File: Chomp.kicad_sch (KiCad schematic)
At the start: 47 parts, among them J1 IN2, J10 V1-6, J11 V1-8, J12 V2-5, J13 V2-8, J14 V2-4, J15 T1-4, J16 T1-2, J2 IN1, J3 V1-2, J4 V1-1, J5 V1-3, J6 RV1-1, J7 RV1-3, J8 RV1-2, J9 V1-7

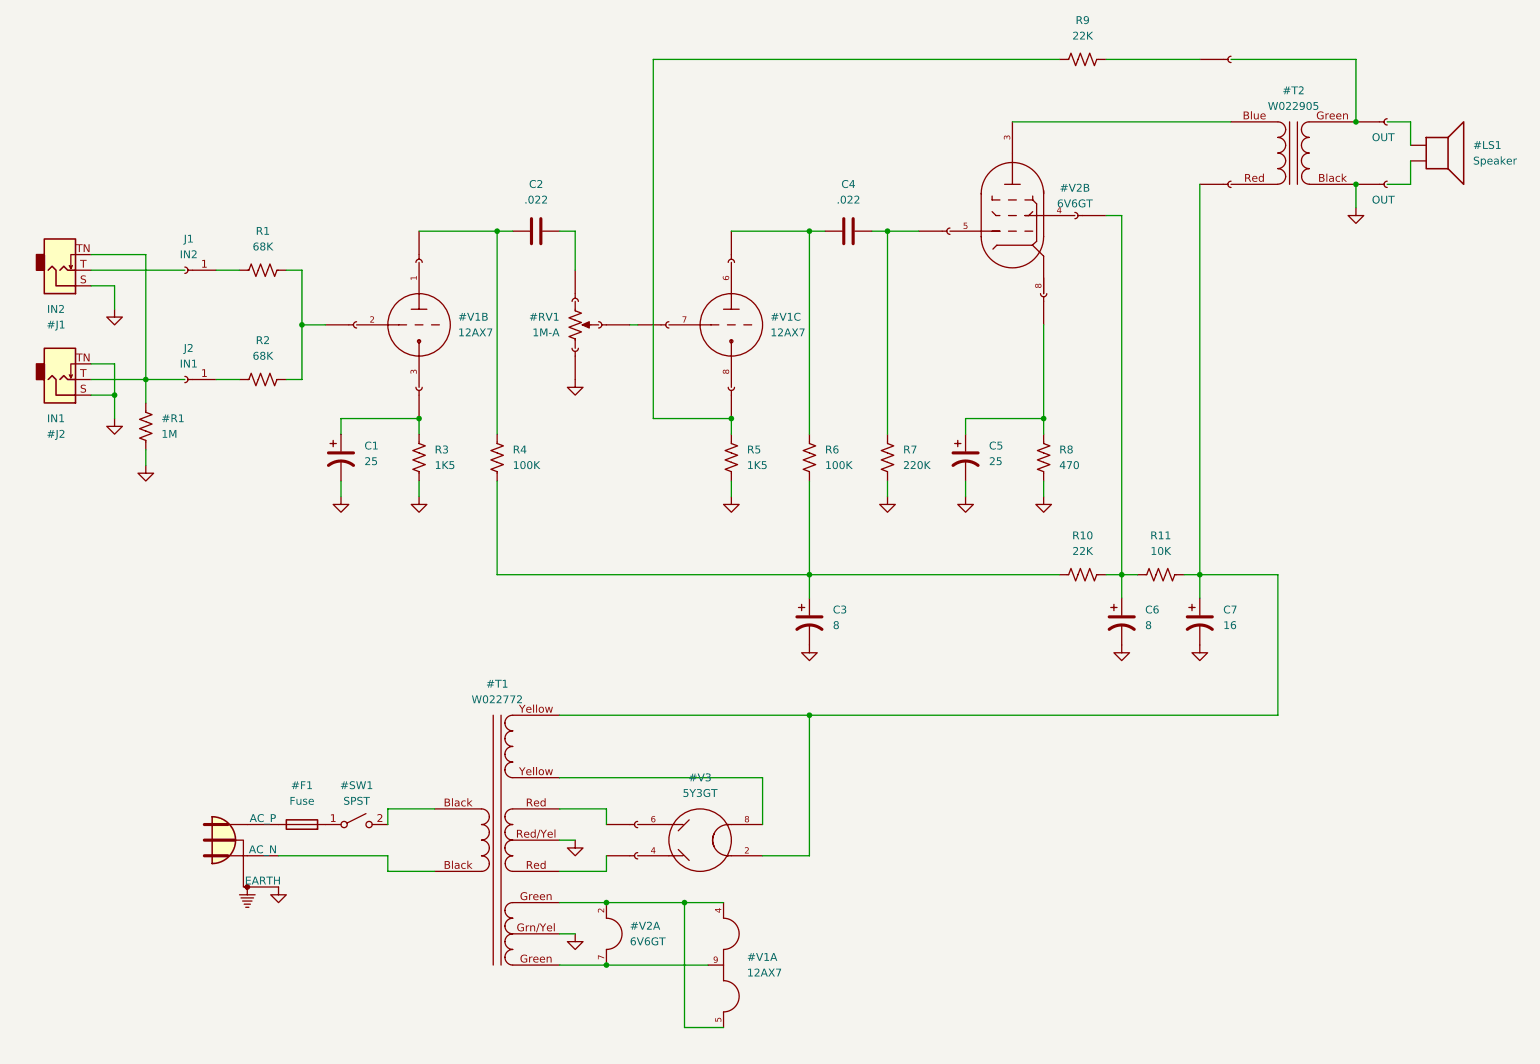
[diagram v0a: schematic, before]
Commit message: Ground routing and layout tweaks.
http://www.valvewizard.co.uk/Grounding.pdf gives some good advice on grounding using a Champ circuit as an example. Rather than leave the schematic ambigous on this topic, I've drawn Blencowe's recommendations directly. The layout matches the schematic almost exactly, though the ordering of the elecrolytic grounds is constrained by reality, and the output ground is tied where convenient.
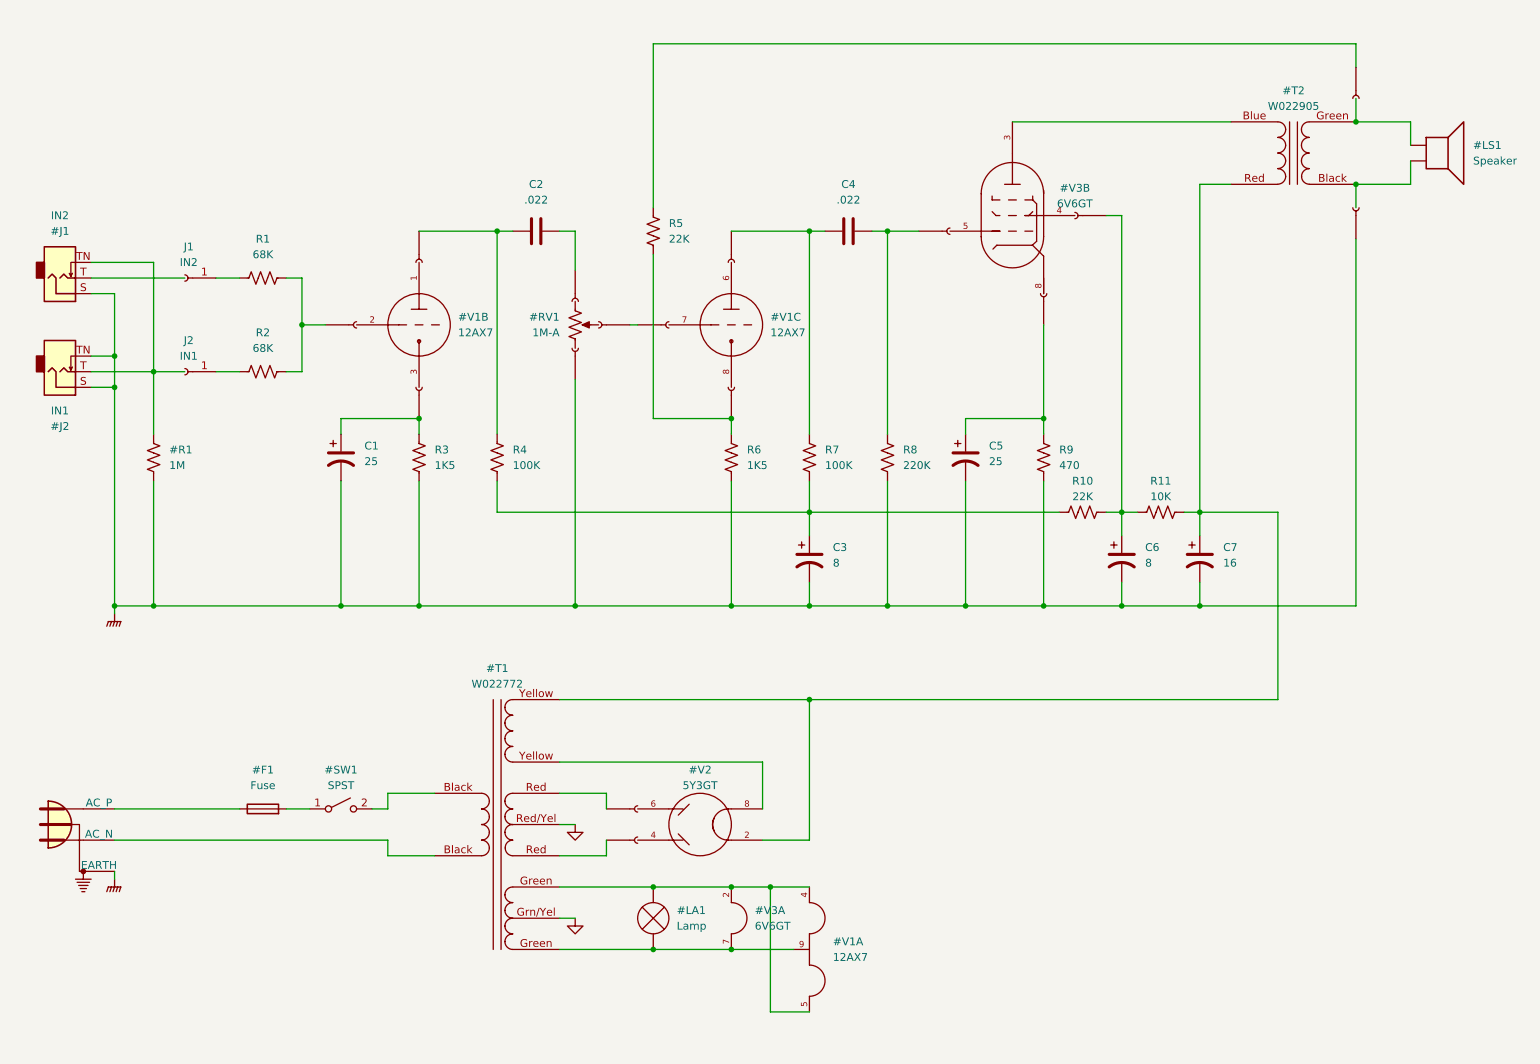
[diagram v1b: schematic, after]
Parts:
- added #LA1: Lamp, symbol Device:Lamp
- J15: value T1-4 -> T2-G
- J16: value T1-2 -> T2-B
- renumbered #V3 to #V2, #V2 to #V3, R9 to R5, R5 to R6, R6 to R7, R7 to R8, R8 to R9
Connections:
- net GND: no longer #J1.S, #J2.S, #J2.TN, #P1.3 (EARTH), #R1.2, #T2.Black (SA), C1.2, C3.2, C5.2, C6.2, C7.2, J7.1 (Pin_1), R3.2, R6.2, R8.2, R9.2
- net at #T1.Yellow (OUT2B), #V2.2 (H1), C7.1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: now also #T2.Red (AB); no longer J16.1 (Pin_1)
- net at #T1.Green (OUT3B), #V1.4 (H1), #V1.5 (H3)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: now also #LA1.2 (+)
- net at #T1.Green (OUT3B), #V1.9 (H2), #V3.7 (H2): now also #LA1.1 (-)
- net at #LS1.1: now also #T2.Green (SB)
- net at #LS1.2: now also #T2.Black (SA)
- new net GNDPWR: #J1.S, #J2.S, #J2.TN, #P1.3 (EARTH), #R1.2, C1.2, C3.2, C5.2, C6.2, C7.2, J16.1 (Pin_1), J7.1 (Pin_1), R3.2, R6.2, R8.2, R9.2
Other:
- moved on the sheet: C3, C6, C7, J1, J2, R1, R10, R11, R2, R5

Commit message: Improve labeling.
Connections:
- net at #T1.Red (OUT1B): now also #V2.6 (A2)
- net at #V2.4 (A1): now also #T1.Red (OUT1B)
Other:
- note added: "B+1"
- note added: "B+2"
- note added: "B+3"

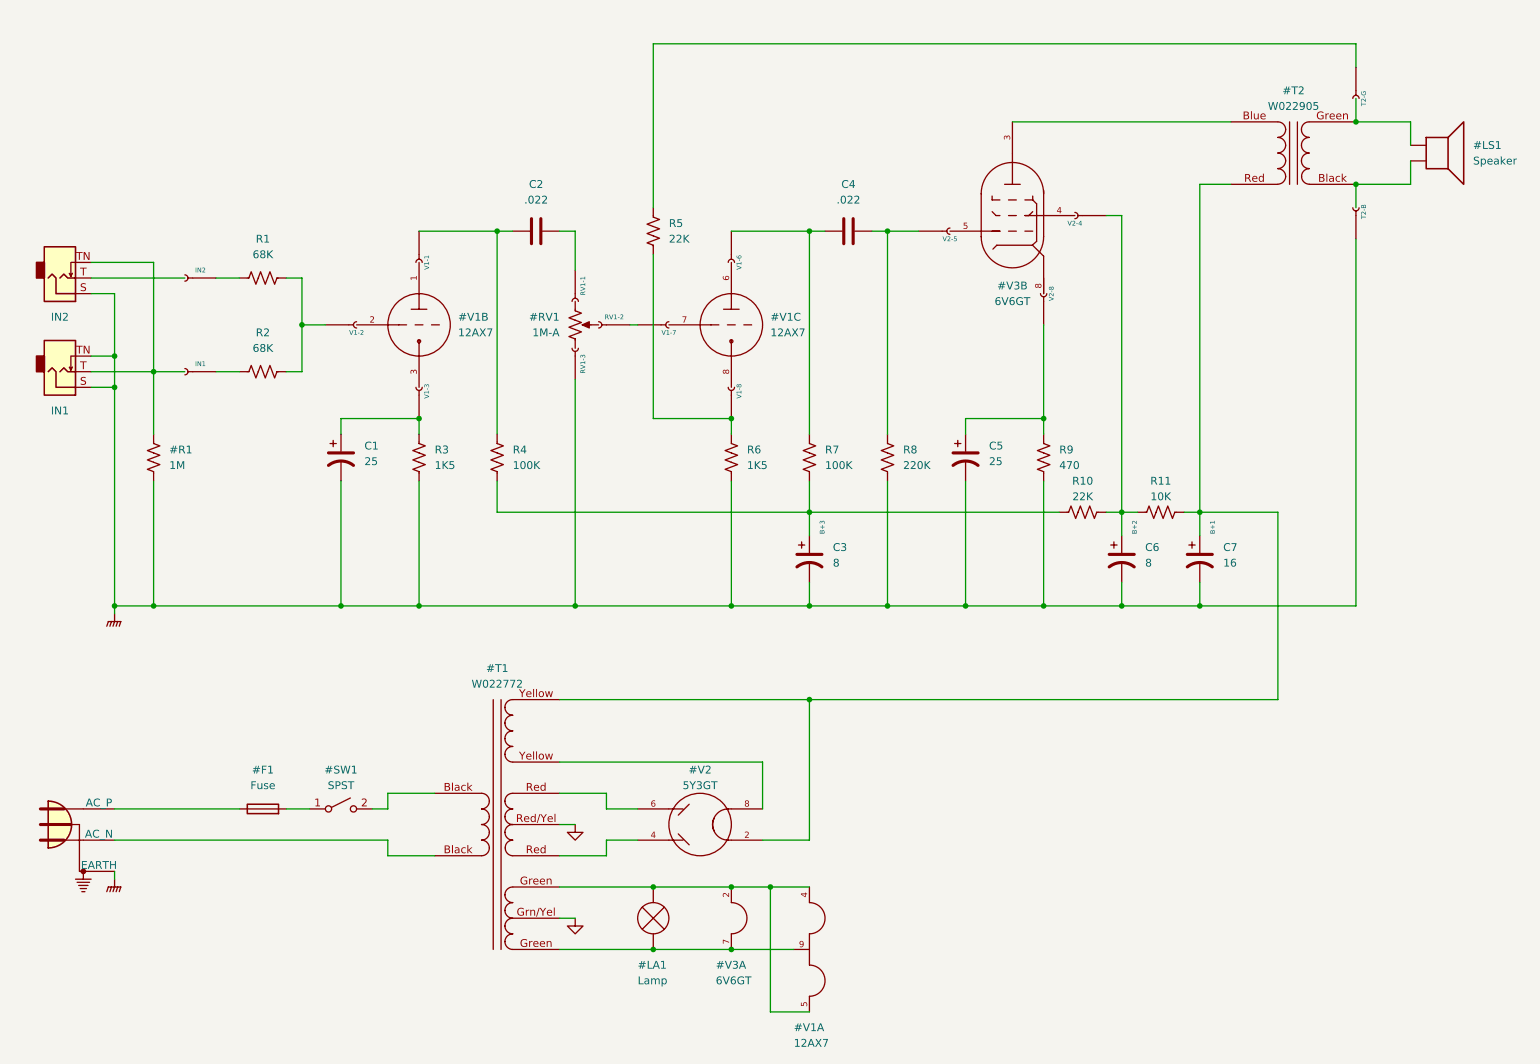
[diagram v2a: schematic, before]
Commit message: Restructure the schematic layout to emphasize power.
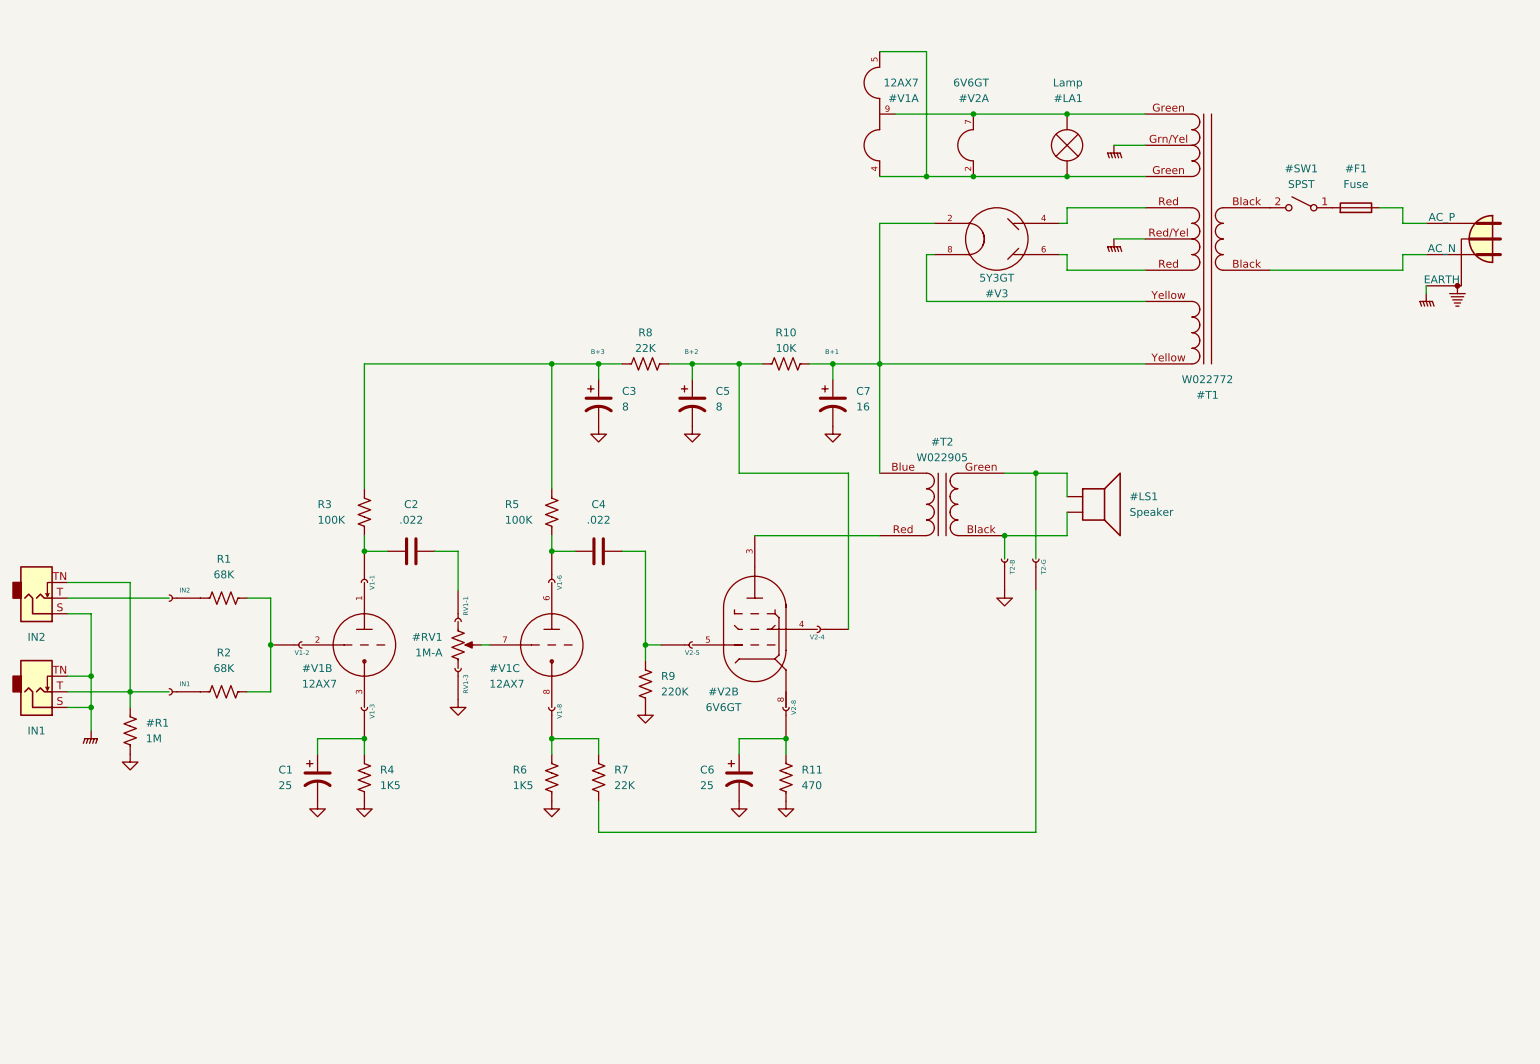
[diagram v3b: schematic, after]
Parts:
- removed J8: RV1-2, Connector_Wire:SolderWire-0.25sqmm_1x01_D0.65mm_OD1.7mm, symbol Connector:Conn_01x01_Female
- removed J9: V1-7, Connector_Wire:SolderWire-0.25sqmm_1x01_D0.65mm_OD1.7mm, symbol Connector:Conn_01x01_Female
- renumbered #V3 to #V2, #V2 to #V3, C6 to C5, C5 to C6, J12 to J10, J13 to J11, J14 to J12, J16 to J13, J15 to J14, J10 to J8, J11 to J9, R11 to R10, R9 to R11, R4 to R3, R3 to R4, R7 to R5, R5 to R7, R10 to R8, R8 to R9
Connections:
- net GND: now also #R1.2, C1.2, C3.2, C5.2, C6.2, C7.2, J13.1 (Pin_1), J7.1 (Pin_1), R11.2, R4.2, R6.2, R9.2; no longer #T1.Grn/Yel (OUT3C), #T1.Red/Yel (OUT1C)
- net GNDPWR: now also #T1.Grn/Yel (OUT3C), #T1.Red/Yel (OUT1C); no longer #R1.2, C1.2, C3.2, C5.2, C6.2, C7.2, J13.1 (Pin_1), J7.1 (Pin_1), R11.2, R4.2, R6.2, R9.2
- net at #T1.Yellow (OUT2B), #V3.2 (H1), C7.1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: now also #T2.Blue (AA); no longer #T2.Red (AB)
- net at #V1.7 (TG): now also #RV1.2
- net at C2.1, J4.1 (Pin_1): now also R3.2; no longer R3.1
- net at C3.1, R8.1: now also R3.1, R5.1; no longer R3.2, R5.2
- net at C4.1, J8.1 (Pin_1): now also R5.2; no longer R5.1
- net at #V2.3 (PA): now also #T2.Red (AB); no longer #T2.Blue (AA)
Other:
- moved on the sheet: C1, C2, C3, C4, C5, C6, C7, R1, R10, R11, R2, R3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

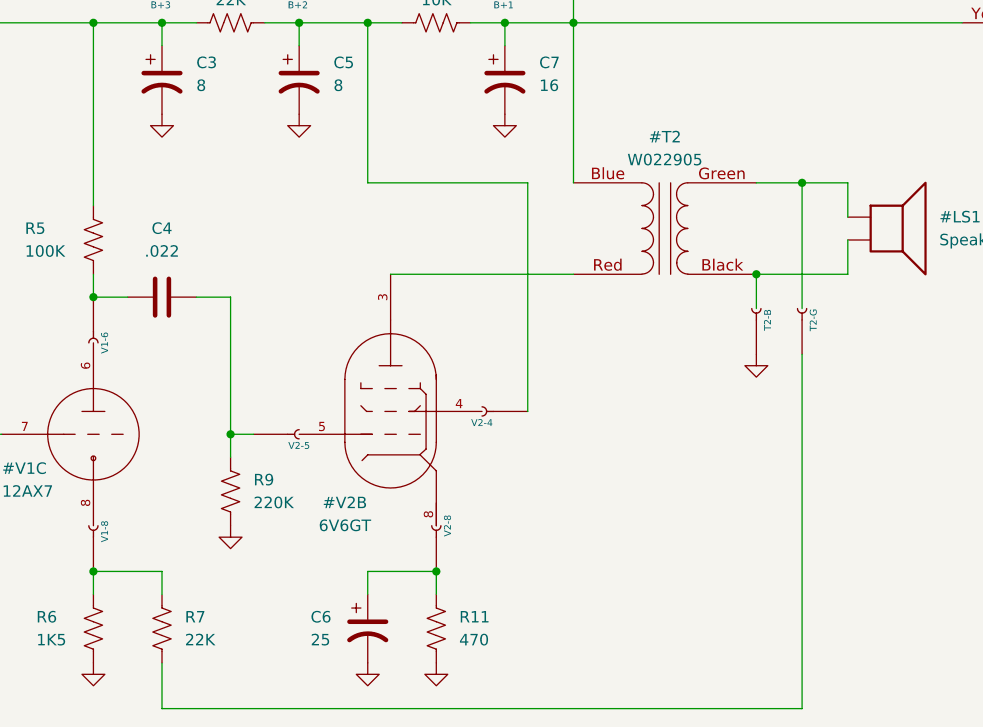
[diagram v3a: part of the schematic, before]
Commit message: Reorient OT and add screen resistor.
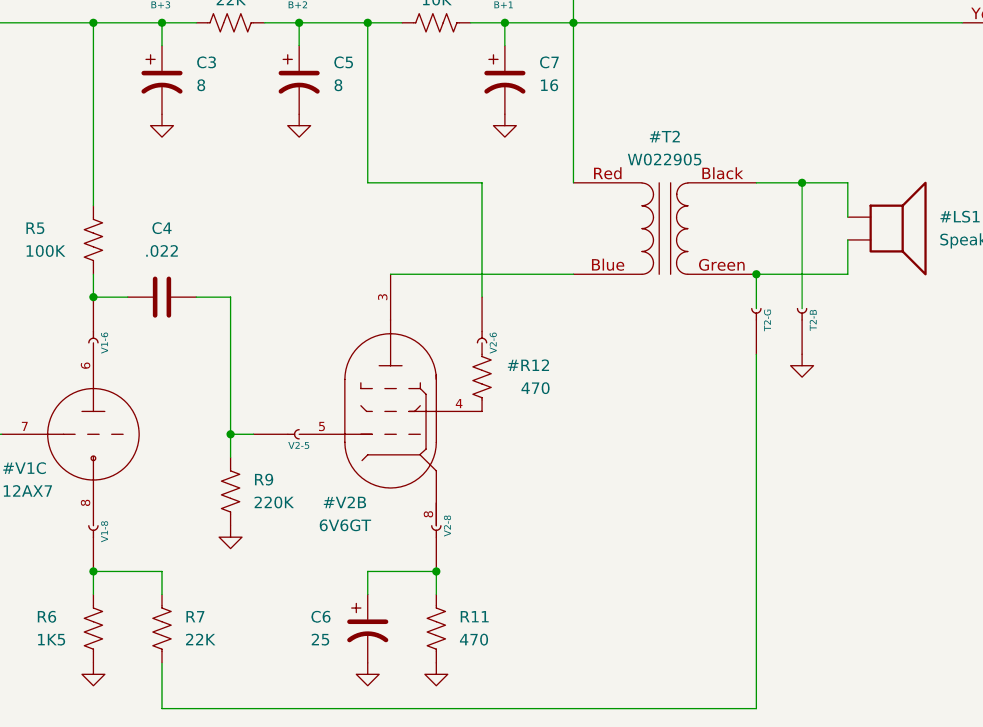
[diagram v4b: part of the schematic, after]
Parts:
- added #R12: 470, Resistor_THT:R_Axial_DIN0411_L9.9mm_D3.6mm_P20.32mm_Horizontal, symbol Device:R_US
- J12: value V2-4 -> V2-6
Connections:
- net at #T1.Yellow (OUT2B), #V3.2 (H1), C7.1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: now also #T2.Red (AB); no longer #T2.Blue (AA)
- net at #LS1.1: now also #T2.Black (SA); no longer #T2.Green (SB)
- net at #LS1.2: now also #T2.Green (SB); no longer #T2.Black (SA)
- net at #V2.3 (PA): now also #T2.Blue (AA); no longer #T2.Red (AB)
- net at #V2.4 (PSG): now also #R12.2

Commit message: Convert to 5E1.
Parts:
- removed R10: 10K, Resistor_THT:R_Axial_DIN0411_L9.9mm_D3.6mm_P20.32mm_Horizontal, symbol Device:R_US
- added #L1: 194A, Inductor_THT:L_Axial_L20.0mm_D8.0mm_P25.40mm_Horizontal, symbol Device:L_Ferrite
- added J11: L1-1, Connector_Wire:SolderWire-0.25sqmm_1x01_D0.65mm_OD1.7mm, symbol Connector:Conn_01x01_Female
- added J13: L1-2, Connector_Wire:SolderWire-0.25sqmm_1x01_D0.65mm_OD1.7mm, symbol Connector:Conn_01x01_Female
- C3, C5: value 8 -> 10
- C7: value 16 -> 15
- renumbered #R12 to #R2, #T2 to #T1, #T1 to #T2, J11 to J12, J12 to J14, J14 to J15, J13 to J16, R11 to R10
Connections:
- net at #T2.Yellow (OUT2B), #V3.2 (H1), C7.1: now also J13.1 (Pin_1); no longer #T1.Red (AB)
- net at #V3.4 (A1): now also #T2.Red/Wht (OUT1B); no longer #T2.Red (OUT1B)
- net at #V3.6 (A2): now also #T2.Red/Wht (OUT1B); no longer #T2.Red (OUT1B)
- net at C5.1, J14.1 (Pin_1), R8.2: now also #T1.Red (AB), J11.1 (Pin_1)
